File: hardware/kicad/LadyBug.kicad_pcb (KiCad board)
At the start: 2 copper layers, 36 x 30 mm, 12 parts, among them IC1 ATTINY85-S, P1 CONN_5, P2 CONN_2, U1 WS2812B

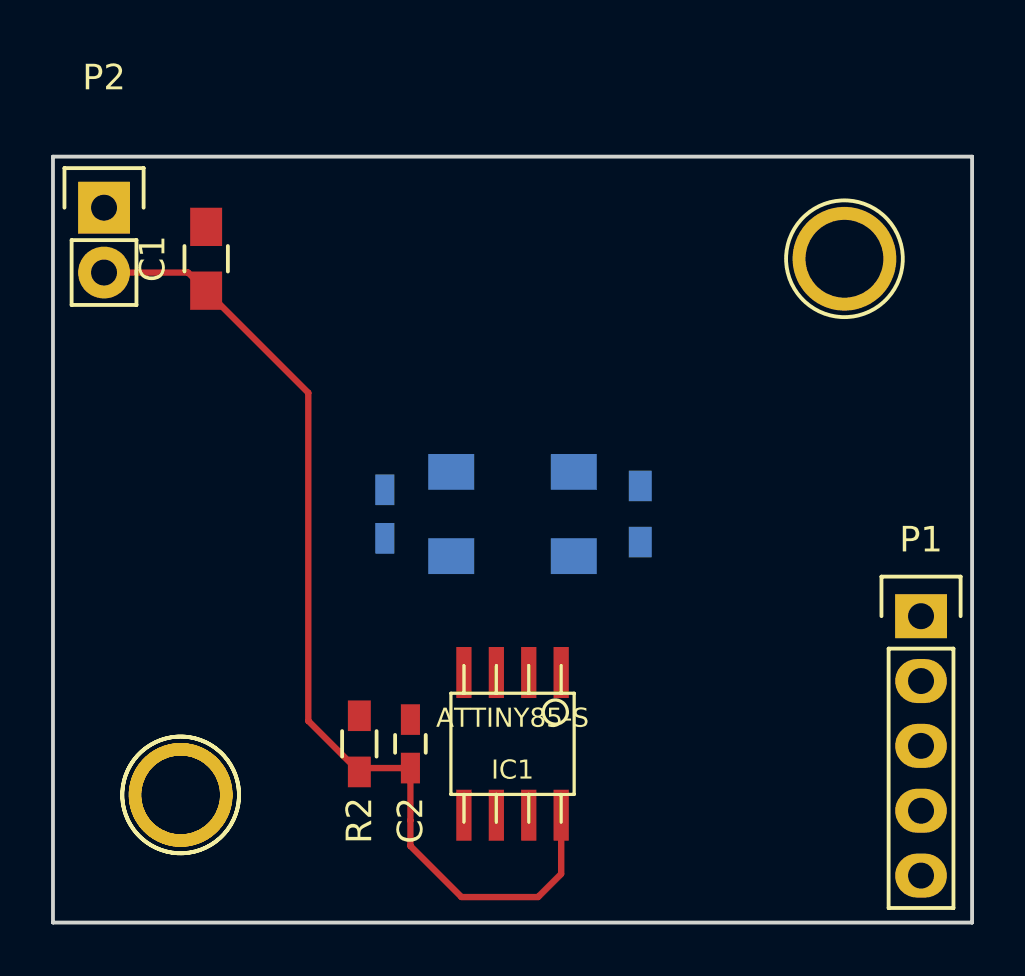
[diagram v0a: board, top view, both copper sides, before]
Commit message: Oops, swapped front and back.
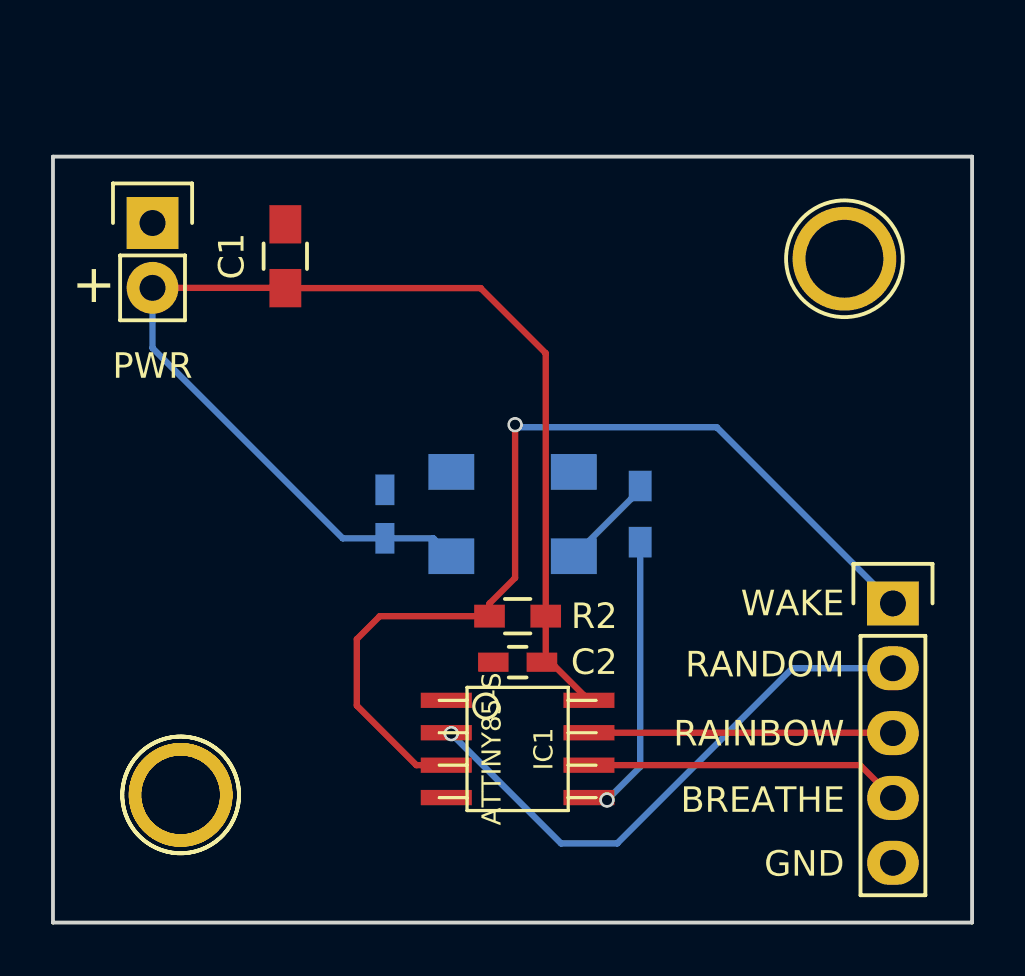
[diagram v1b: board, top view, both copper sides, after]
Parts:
- moved R2 7.96 mm to (118.2, 118.0), turned to 180 degrees
- moved C2 5.28 mm to (118.2, 119.8), turned to 180 degrees
- moved C1 3.10 mm to (109.1, 103.9)
- moved PWR 1.99 mm to (103.9, 102.6)
- moved P1 1.21 mm to (132.9, 117.5)
- moved IC1 0.28 mm to (118.2, 123.2), turned to 270 degrees
- turned C3 to 270 degrees
- renumbered P2 to PWR
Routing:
- net Net-(IC1-Pad3): track 0.00 -> 39.2 mm, vias 0 -> 1
- net Net-(IC1-Pad2): track 0.00 -> 22.1 mm, vias 0 -> 1
- net Net-(IC1-Pad6): track 0.00 -> 13.1 mm
- net Net-(IC1-Pad7): track 0.00 -> 12.5 mm
- net Net-(IC1-Pad5): track 0.00 -> 11.4 mm, vias 0 -> 1
- net +5V: track 40.0 -> 48.4 mm
- net Net-(R1-Pad2): track 0.00 -> 3.83 mm
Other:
- board text added: "+"
- board text added: "BREATHE"
- board text added: "GND"
- board text added: "RAINBOW"
- board text added: "RANDOM"
- board text added: "WAKE"

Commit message: Moved some silscreens around.
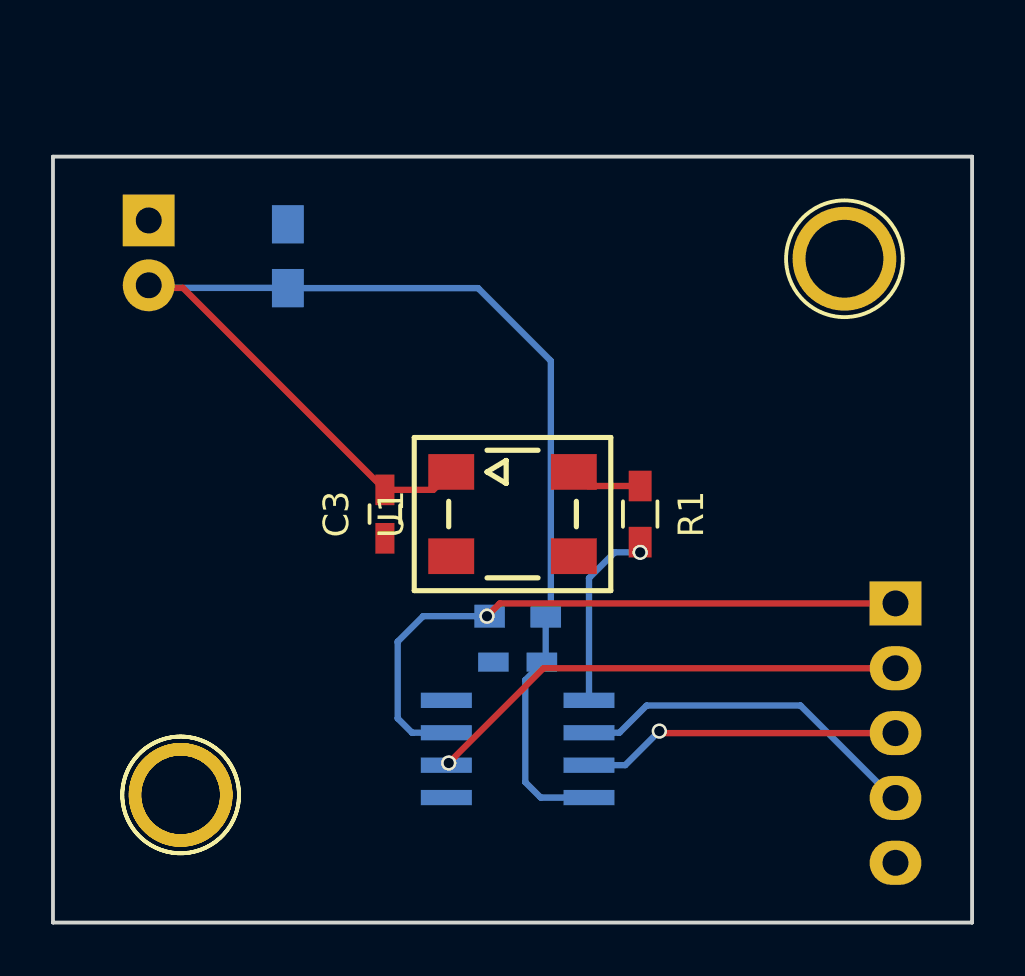
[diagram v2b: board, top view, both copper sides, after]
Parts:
- C1, C2, IC1, P1, PWR, R2: moved to B.Cu
- C3, R1, U1: moved to F.Cu
- moved PWR 0.18 mm to (103.8, 102.5), turned to 180 degrees
- moved C1 0.10 mm to (109.2, 103.9)
- moved P1 0.10 mm to (133.0, 117.5), turned to 180 degrees
- turned C3 to 90 degrees
- turned IC1 to 90 degrees
- turned U1 to 90 degrees
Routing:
- net Net-(IC1-Pad3): track 39.2 -> 25.4 mm
- net Net-(IC1-Pad5): track 11.4 -> 7.61 mm
- net +5V: track 48.4 -> 51.7 mm
- net Net-(IC1-Pad2): track 22.1 -> 19.1 mm
- net Net-(R1-Pad2): track 3.83 -> 2.83 mm
- net Net-(IC1-Pad6): track 13.1 -> 13.8 mm
- net Net-(IC1-Pad7): vias 0 -> 1

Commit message: Some ladybug tweaking, v1 of board DOA.
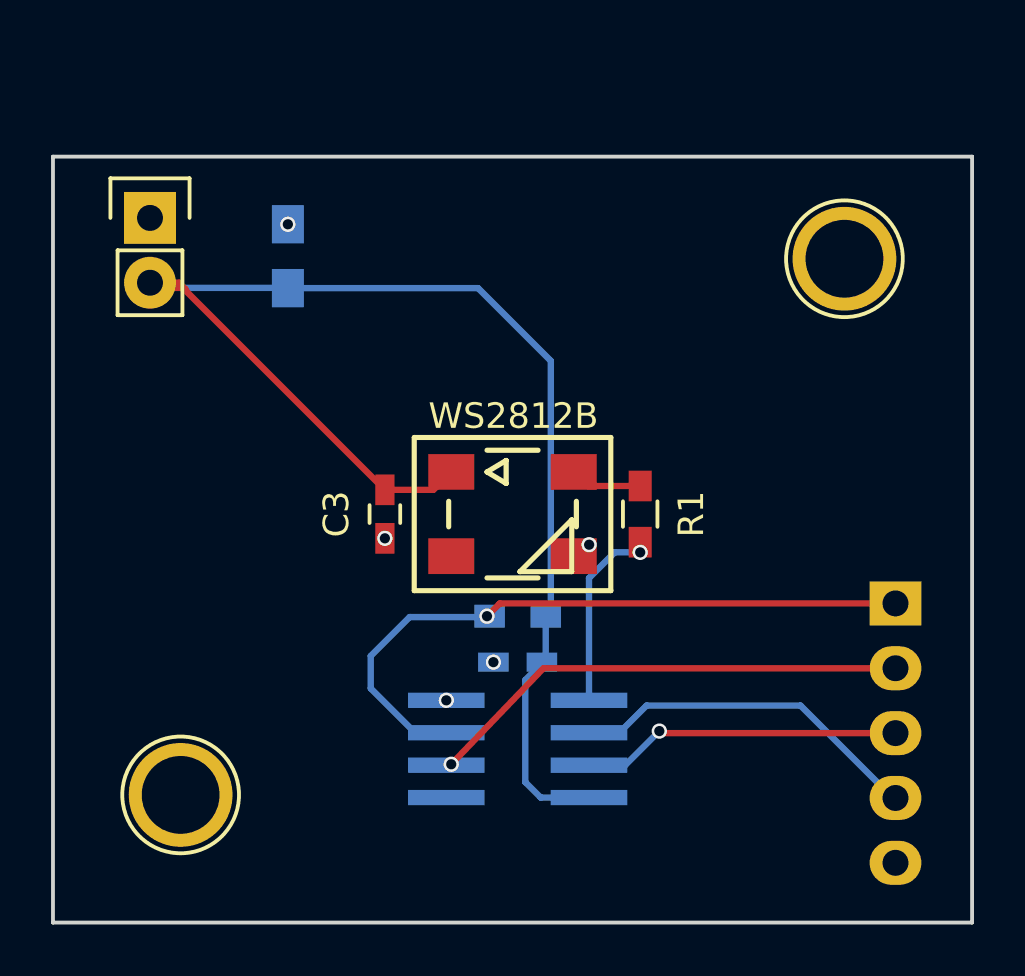
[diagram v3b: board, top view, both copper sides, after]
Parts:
- removed ?: 1pin, Connect:1pin
- removed PWR: CONN_2, Pin_Headers:Pin_Header_Straight_1x02
- added P2: CONN_2, Pin_Headers:Pin_Header_Straight_1x02, F.Cu at (103.8, 102.4)
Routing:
- net Net-(IC1-Pad3): track 25.4 -> 27.8 mm
- net +5V: track 51.7 -> 53.3 mm
- net GND: track 0.00 -> 1.03 mm, vias 0 -> 5
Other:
- board text added: "PWR"
- board text added: "WS2812B"

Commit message: Added some more silkscreening.
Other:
- board text added: "LadyBug85 v0.2"
- board text added: "z2amiller"
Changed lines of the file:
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@@
     (area 99.924999 99.924999 136.075001 130.075001)
     (thickness 1.6)
-    (drawings 15)
+    (drawings 17)
     (tracks 64)
     (zones 0)
@@
     )
   )
+  (gr_text z2amiller (at 134.4 111 90) (layer B.SilkS)
+    (effects (font (size 1 1) (thickness 0.25)) (justify mirror))
+  )
+  (gr_text "LadyBug85 v0.2" (at 119.4 101.8) (layer B.SilkS)
+    (effects (font (size 1.25 1.25) (thickness 0.3)) (justify mirror))
+  )
   (gr_text PWR (at 103.6 107.8) (layer B.SilkS)
     (effects (font (size 1.5 1.5) (thickness 0.3)) (justify mirror))
@@
   (gr_line (start 100 130) (end 136 130) (angle 90) (layer Edge.Cuts) (width 0.15))
   (gr_line (start 100 100) (end 100 130) (angle 90) (layer Edge.Cuts) (width 0.15))
-  (segment (start 103.8 104.94) (end 104.94 104.94) (width 0.25) (layer F.Cu) (net 1) (status 400000))
+  (segment (start 103.8 104.94) (end 104.94 104.94) (width 0.25) (layer F.Cu) (net 1))
   (segment (start 105.2 105.2) (end 105.2 105.25) (width 0.25) (layer F.Cu) (net 1))
   (segment (start 104.94 104.94) (end 105.2 105.2) (width 0.25) (layer F.Cu) (net 1))
@@
   (segment (start 103.9 105.14) (end 109.19 105.14) (width 0.25) (layer B.Cu) (net 1))
   (segment (start 109.19 105.14) (end 109.2 105.15) (width 0.25) (layer B.Cu) (net 1))
-  (via (at 109.2 102.65) (size 0.6) (drill 0.4) (layers F.Cu B.Cu) (net 2) (status 400000))
+  (via (at 109.2 102.65) (size 0.6) (drill 0.4) (layers F.Cu B.Cu) (net 2))
   (segment (start 109.2 102.65) (end 109.2 102.6) (width 0.25) (layer F.Cu) (net 2))
-  (via (at 121 115.2) (size 0.6) (drill 0.4) (layers F.Cu B.Cu) (net 2) (status 800000))
-  (segment (start 121 115.2) (end 120.55 115.65) (width 0.25) (layer F.Cu) (net 2) (status C00000))
-  (segment (start 120.55 115.65) (end 120.4 115.65) (width 0.25) (layer F.Cu) (net 2) (status C00000))
-  (via (at 113 114.95) (size 0.6) (drill 0.4) (layers F.Cu B.Cu) (net 2) (status C00000))
-  (segment (start 113 114.95) (end 113 115) (width 0.25) (layer B.Cu) (net 2) (status 400000))
-  (via (at 117.25 119.8) (size 0.6) (drill 0.4) (layers F.Cu B.Cu) (net 2) (status 400000))
+  (via (at 121 115.2) (size 0.6) (drill 0.4) (layers F.Cu B.Cu) (net 2))
+  (segment (start 121 115.2) (end 120.55 115.65) (width 0.25) (layer F.Cu) (net 2))
+  (segment (start 120.55 115.65) (end 120.4 115.65) (width 0.25) (layer F.Cu) (net 2))
+  (via (at 113 114.95) (size 0.6) (drill 0.4) (layers F.Cu B.Cu) (net 2))
+  (segment (start 113 114.95) (end 113 115) (width 0.25) (layer B.Cu) (net 2))
+  (via (at 117.25 119.8) (size 0.6) (drill 0.4) (layers F.Cu B.Cu) (net 2))
   (segment (start 117.25 119.8) (end 117.2 119.8) (width 0.25) (layer F.Cu) (net 2))
-  (via (at 115.406 121.295) (size 0.6) (drill 0.4) (layers F.Cu B.Cu) (net 2) (status 400000))
+  (via (at 115.406 121.295) (size 0.6) (drill 0.4) (layers F.Cu B.Cu) (net 2))
   (segment (start 115.4 121.2) (end 115.4 121.289) (width 0.25) (layer F.Cu) (net 2))
   (segment (start 115.4 121.289) (end 115.406 121.295) (width 0.25) (layer F.Cu) (net 2))

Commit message: Changed silkscreen to match version 2.1.
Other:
- board text added: "LadyBug85 v2.1"
- board text removed: "LadyBug85 v0.2"
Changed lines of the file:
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@@
     (links 19)
     (no_connects 0)
-    (area 99.924999 99.924999 136.075001 130.075001)
+    (area 99.924999 98.175 136.203572 130.075001)
     (thickness 1.6)
     (drawings 17)
@@
     (effects (font (size 1 1) (thickness 0.25)) (justify mirror))
   )
-  (gr_text "LadyBug85 v0.2" (at 119.4 101.8) (layer B.SilkS)
+  (gr_text "LadyBug85 v2.1" (at 119.4 101.8) (layer B.SilkS)
     (effects (font (size 1.25 1.25) (thickness 0.3)) (justify mirror))
   )
